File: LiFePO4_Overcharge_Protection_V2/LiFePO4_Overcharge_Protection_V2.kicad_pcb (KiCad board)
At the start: 2 copper layers, 70 x 35 mm, 39 parts, among them J1 Conn_01x02_Pin, J2 Conn_01x02_Pin, J3 Conn_01x02_Pin, J4 Conn_01x02_Pin, J5 Conn_01x01_Pin, J6 Conn_01x01_Pin, J7 Conn_01x01_Pin, J8 Conn_01x01_Pin, Q1 Q_NPN_EBC, Q2 Q_PNP_EBC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

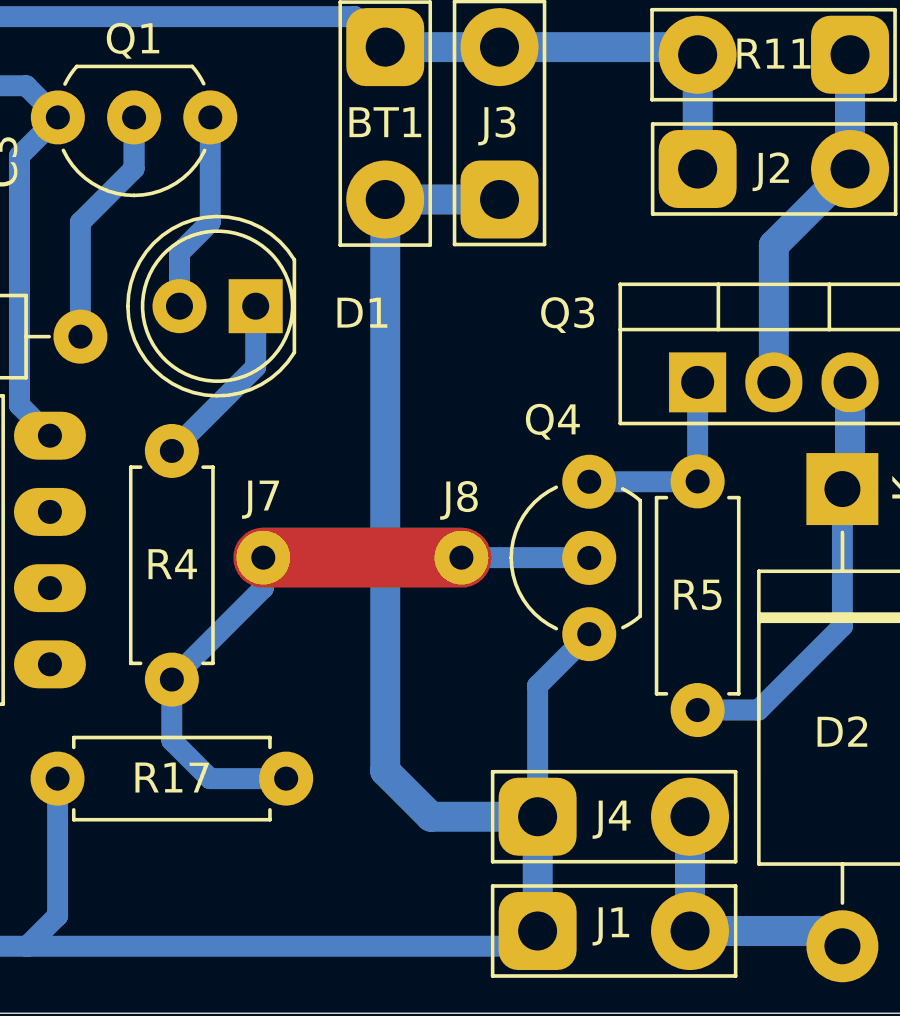
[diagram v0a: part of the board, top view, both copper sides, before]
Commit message: add LiFePO4_Overcharge_Protection_V2 and MOSFET_Switch
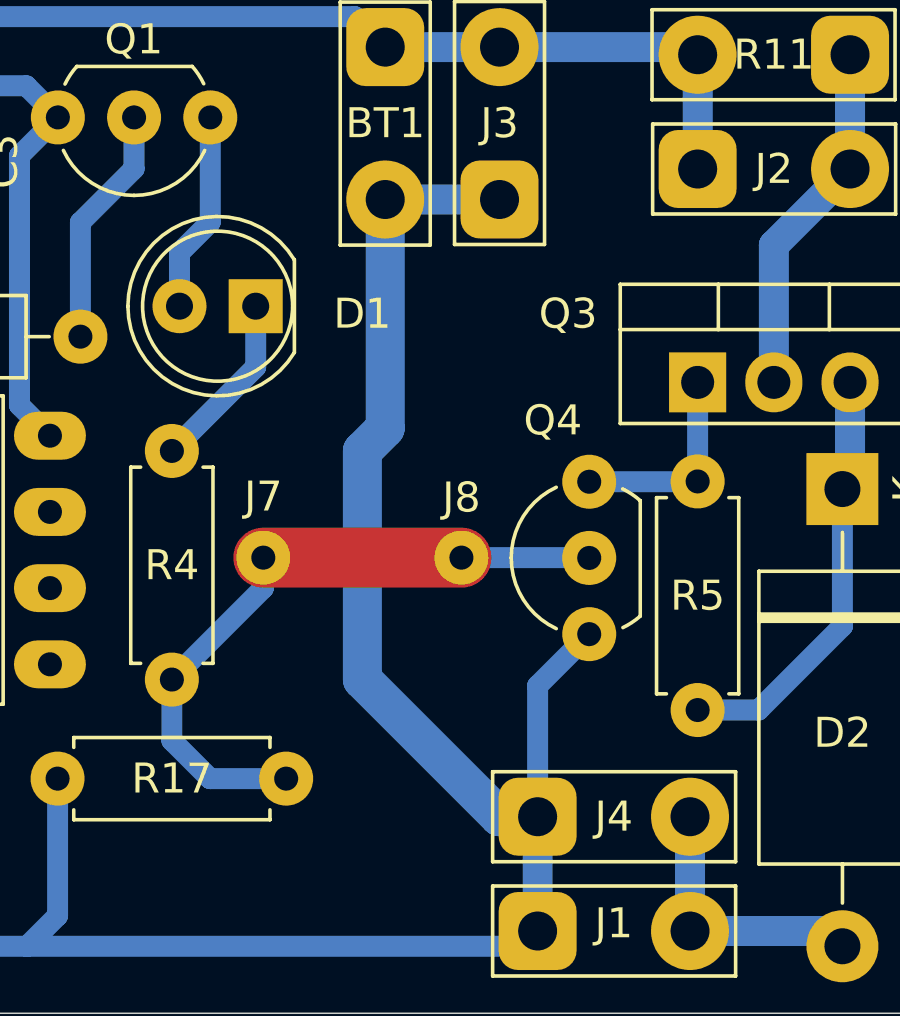
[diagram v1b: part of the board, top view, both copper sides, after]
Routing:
- net GND: track 172.4 -> 171.7 mm
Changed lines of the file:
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@@
 		(allow_soldermask_bridges_in_footprints no)
 		(pcbplotparams
-			(layerselection 0x00010fc_ffffffff)
+			(layerselection 0x0000000_7fffffff)
 			(plot_on_all_layers_selection 0x0000000_00000000)
 			(disableapertmacros no)
@@
 			(pdf_back_fp_property_popups yes)
 			(dxfpolygonmode yes)
-			(dxfimperialunits yes)
+			(dxfimperialunits no)
 			(dxfusepcbnewfont yes)
 			(psnegative no)
@@
 			(sketchpadsonfab no)
 			(subtractmaskfromsilk no)
-			(outputformat 1)
+			(outputformat 3)
 			(mirror no)
-			(drillshape 1)
+			(drillshape 0)
 			(scaleselection 1)
 			(outputdirectory "")
@@
 		(tags "TO-92L Inline Wide transistor")
 		(property "Reference" "U1"
-			(at 2.54 -3.56 360)
+			(at 2.54 -3.56 0)
 			(layer "F.SilkS")
 			(hide yes)
@@
 		)
 		(property "Value" "TL431LP"
-			(at 2.54 2.79 360)
+			(at 2.54 2.79 0)
 			(layer "F.Fab")
 			(effects
@@
 		)
 		(fp_text user "${REFERENCE}"
-			(at 2.54 0 360)
+			(at 2.54 0 0)
 			(layer "F.Fab")
 			(effects
@@
 		(tags "Resistor Axial_DIN0207 series Axial Horizontal pin pitch 7.62mm 0.25W = 1/4W length 6.3mm diameter 2.5mm")
 		(property "Reference" "R1"
-			(at 3.81 0 360)
+			(at 3.81 0 0)
 			(layer "F.SilkS")
 			(hide yes)
@@
 		)
 		(property "Value" "4.7k"
-			(at 3.81 2.37 360)
+			(at 3.81 2.37 0)
 			(layer "F.Fab")
 			(effects
@@
 		)
 		(fp_text user "${REFERENCE}"
-			(at 3.81 0 360)
+			(at 3.81 0 0)
 			(layer "F.Fab")
 			(effects
@@
 	)
 	(segment
+		(start 170.942 46.736)
+		(end 170.942 54.356)
+		(width 1.3)
+		(layer "B.Cu")
+		(net 2)
+	)
+	(segment
 		(start 139.446 71.628)
 		(end 138.43 70.612)
@@
 	)
 	(segment
+		(start 174.752 67.31)
+		(end 176.022 67.31)
+		(width 1.3)
+		(layer "B.Cu")
+		(net 2)
+	)
+	(segment
 		(start 139.954 71.628)
 		(end 139.446 71.628)
@@
 	)
 	(segment
-		(start 170.942 46.736)
-		(end 170.942 65.786)
-		(width 1)
-		(layer "B.Cu")
-		(net 2)
-	)
-	(segment
 		(start 160.02 70.612)
 		(end 159.004 71.628)
@@
 	)
 	(segment
-		(start 170.942 65.786)
-		(end 172.466 67.31)
-		(width 1)
-		(layer "B.Cu")
-		(net 2)
-	)
-	(segment
 		(start 129.286 52.07)
 		(end 129.286 51.816)
@@
 	)
 	(segment
+		(start 170.18 55.118)
+		(end 170.18 62.738)
+		(width 1.3)
+		(layer "B.Cu")
+		(net 2)
+	)
+	(segment
 		(start 127.508 53.848)
 		(end 127.508 61.722)
@@
 	)
 	(segment
-		(start 172.466 67.31)
-		(end 176.022 67.31)
-		(width 1)
-		(layer "B.Cu")
-		(net 2)
-	)
-	(segment
 		(start 155.956 62.23)
 		(end 156.718 62.992)
@@
 		(layer "B.Cu")
 		(net 2)
+	)
+	(segment
+		(start 170.942 54.356)
+		(end 170.18 55.118)
+		(width 1.3)
+		(layer "B.Cu")
+		(net 2)
+	)
+	(segment
+		(start 170.18 62.738)
+		(end 174.752 67.31)
+		(width 1.3)
+		(layer "B.Cu")
+		(net 2)
